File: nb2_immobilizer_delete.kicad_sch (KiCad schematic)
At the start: 6 parts, among them J1 AVR-ISP-6, Q1 BC849, Q2 BC849, U1 ATtiny85-20S

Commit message: first draft
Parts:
- added P1: 1123038-2, 1123038-2:1123038-2, symbol 1123038-2:1123038-2
- J1: footprint Package_SO:SOIC-20W_7.5x12.8mm_P1.27mm -> Connector:Tag-Connect_TC2030-IDC-NL_2x03_P1.27mm_Vertical
- Q1, Q2: LCSC Part # (none) -> C334244
- R1: footprint Resistor_THT:R_Array_SIP4 -> Resistor_SMD:R_0603_1608Metric; LCSC Part # (none) -> C22807
- R2: footprint Resistor_THT:R_Array_SIP4 -> Resistor_SMD:R_0603_1608Metric; LCSC Part # (none) -> C22843
- U1: LCSC Part # (none) -> C31540447
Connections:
- net +5V: now also P1.66 (4L)
- net GND: now also P1.64 (4A)
- net bus: now also P1.36 (3S)
- net cluster: no longer names the net of U1.3 (XTAL2/PB4)
- net led renamed PB1
- no-connect marks 1 -> 71
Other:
- moved on the sheet: J1, Q1, Q2, R1, R2, U1

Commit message: added capacitor, dnp tag-connect
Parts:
- added C1: 100nf, Capacitor_SMD:C_0603_1608Metric, symbol Device:C_Small
- J1: now left out of the parts list
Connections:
- net +5V: now also C1.1
- net GND: now also C1.2
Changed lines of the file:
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@@
 		(body_style 1)
 		(exclude_from_sim no)
-		(in_bom yes)
-		(on_board yes)
-		(in_pos_files yes)
+		(in_bom no)
+		(on_board yes)
+		(in_pos_files no)
 		(dnp no)
 		(property "Reference" "J1"
@@
 				(path "/20eccbaf-1c27-4c38-b279-b161e9ceabac"
 					(reference "J1")
+					(unit 1)
+				)
+			)
+		)
+	)
+	(symbol
+		(lib_id "Device:C_Small")
+		(at 52.07 54.61 0)
+		(unit 1)
+		(body_style 1)
+		(exclude_from_sim no)
+		(in_bom yes)
+		(on_board yes)
+		(in_pos_files yes)
+		(dnp no)
+		(fields_autoplaced yes)
+		(property "Reference" "C1"
+			(at 54.61 53.3399 0)
+			(show_name no)
+			(do_not_autoplace no)
+			(effects
+				(font
+					(size 1.27 1.27)
+				)
+				(justify left)
+			)
+		)
+		(property "Value" "100nf"
+			(at 54.61 55.8799 0)
+			(show_name no)
+			(do_not_autoplace no)
+			(effects
+				(font
+					(size 1.27 1.27)
+				)
+				(justify left)
+			)
+		)
+		(property "Footprint" "Capacitor_SMD:C_0603_1608Metric"
+			(at 52.07 54.61 0)
+			(hide yes)
+			(show_name no)
+			(do_not_autoplace no)
+			(effects
+				(font
+					(size 1.27 1.27)
+				)
+			)
+		)
+		(property "Datasheet" ""
+			(at 52.07 54.61 0)
+			(hide yes)
+			(show_name no)
+			(do_not_autoplace no)
+			(effects
+				(font
+					(size 1.27 1.27)
+				)
+			)
+		)
+		(property "Description" "Unpolarized capacitor, small symbol"
+			(at 52.07 64.77 0)
+			(hide yes)
+			(show_name no)
+			(do_not_autoplace no)
+			(effects
+				(font
+					(size 1.27 1.27)
+				)
+			)
+		)
+		(pin "1"
+		)
+		(pin "2"
+		)
+		(instances
+			(project "nb2_immobilizer_delete"
+				(path "/20eccbaf-1c27-4c38-b279-b161e9ceabac"
+					(reference "C1")
 					(unit 1)
 				)
@@
 	)
 	(symbol
+		(lib_id "power:GND")
+		(at 52.07 57.15 0)
+		(unit 1)
+		(body_style 1)
+		(exclude_from_sim no)
+		(in_bom yes)
+		(on_board yes)
+		(in_pos_files yes)
+		(dnp no)
+		(fields_autoplaced yes)
+		(property "Reference" "#PWR010"
+			(at 52.07 63.5 0)
+			(hide yes)
+			(show_name no)
+			(do_not_autoplace no)
+			(effects
+				(font
+					(size 1.27 1.27)
+				)
+			)
+		)
+		(property "Value" "GND"
+			(at 52.07 62.23 0)
+			(show_name no)
+			(do_not_autoplace no)
+			(effects
+				(font
+					(size 1.27 1.27)
+				)
+			)
+		)
+		(property "Footprint" ""
+			(at 52.07 57.15 0)
+			(hide yes)
+			(show_name no)
+			(do_not_autoplace no)
+			(effects
+				(font
+					(size 1.27 1.27)
+				)
+			)
+		)
+		(property "Datasheet" ""
+			(at 52.07 57.15 0)
+			(hide yes)
+			(show_name no)
+			(do_not_autoplace no)
+			(effects
+				(font
+					(size 1.27 1.27)
+				)
+			)
+		)
+		(property "Description" "Power symbol creates a global label with name \"GND\" , ground"
+			(at 52.07 57.15 0)
+			(hide yes)
+			(show_name no)
+			(do_not_autoplace no)
+			(effects
+				(font
+					(size 1.27 1.27)
+				)
+			)
+		)
+		(pin "1"
+		)
+		(instances
+			(project "nb2_immobilizer_delete"
+				(path "/20eccbaf-1c27-4c38-b279-b161e9ceabac"
+					(reference "#PWR010")
+					(unit 1)
+				)
+			)
+		)
+	)
+	(symbol
 		(lib_id "Device:R_Small")
 		(at 96.52 57.15 180)
@@
 					(unit 1)
 				)
+			)
+		)
+	)
+	(symbol
+		(lib_id "power:+5V")
+		(at 52.07 52.07 0)
+		(unit 1)
+		(body_style 1)
+		(exclude_from_sim no)
+		(in_bom yes)
+		(on_board yes)
+		(in_pos_files yes)
+		(dnp no)
+		(fields_autoplaced yes)
+		(property "Reference" "#PWR09"
+			(at 52.07 55.88 0)
+			(hide yes)
+			(show_name no)
+			(do_not_autoplace no)
+			(effects
+				(font
+					(size 1.27 1.27)
+				)
+			)
+		)
+		(property "Value" "+5V"
+			(at 52.07 46.99 0)
+			(show_name no)
+			(do_not_autoplace no)
+			(effects
+				(font
+					(size 1.27 1.27)
+				)
+			)
+		)
+		(property "Footprint" "Package_SO:SOIC-8_5.3x5.3mm_P1.27mm"
+			(at 52.07 52.07 0)
+			(hide yes)
+			(show_name no)
+			(do_not_autoplace no)
+			(effects
+				(font
+					(size 1.27 1.27)
+				)
+			)
+		)
+		(property "Datasheet" ""
+			(at 52.07 52.07 0)
+			(hide yes)
+			(show_name no)
+			(do_not_autoplace no)
+			(effects
+				(font
+					(size 1.27 1.27)
+				)
+			)
+		)
+		(property "Description" "Power symbol creates a global label with name \"+5V\""
+			(at 52.07 52.07 0)
+			(hide yes)
+			(show_name no)
+			(do_not_autoplace no)
+			(effects
+				(font
+					(size 1.27 1.27)
+				)
+			)
+		)
+		(pin "1"
+		)
+		(instances
+			(project "nb2_immobilizer_delete"
+				(path "/20eccbaf-1c27-4c38-b279-b161e9ceabac"
+					(reference "#PWR09")
+					(unit 1)
+				)

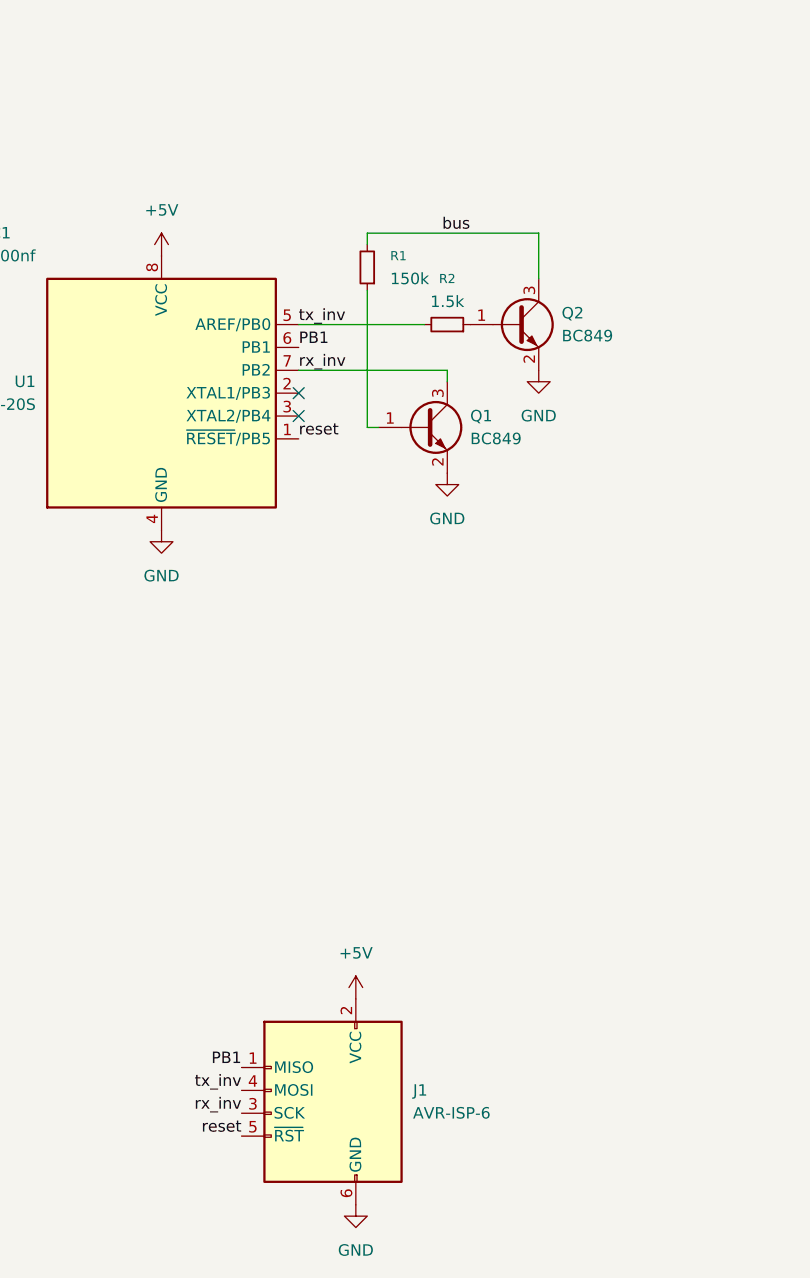
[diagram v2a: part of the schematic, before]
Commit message: revised layout for robustness, reduced clock to 1mhz, added github actions workflow
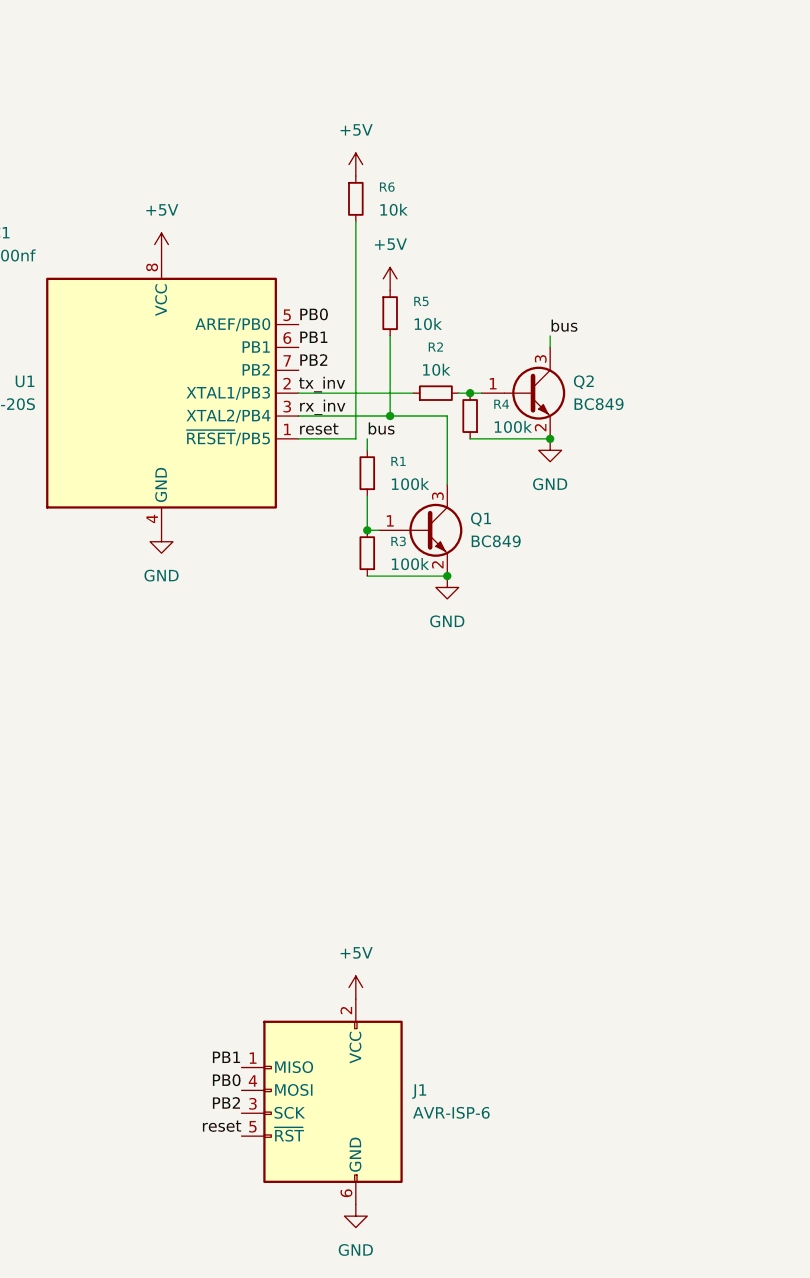
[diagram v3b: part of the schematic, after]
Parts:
- added R3, R4: 100k, Resistor_SMD:R_0603_1608Metric, symbol Device:R_Small
- added R5, R6: 10k, Resistor_SMD:R_0603_1608Metric, symbol Device:R_Small
- R1: value 150k -> 100k; LCSC Part # C22807 -> C25803
- R2: value 1.5k -> 10k; LCSC Part # C22843 -> C25804
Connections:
- net +5V: now also R5.1, R6.1
- net GND: now also R3.1, R4.1
- net reset: now also R6.2
- net rx_inv: now also U1.3 (XTAL2/PB4), R5.2; no longer J1.3 (SCK), U1.7 (PB2)
- net tx_inv: now also R2.1, U1.2 (XTAL1/PB3); no longer J1.4 (MOSI), R2.2, U1.5 (AREF/PB0)
- net at Q2.1 (B): now also R2.2, R4.2; no longer R2.1
- net at Q1.1 (B), R1.1: now also R3.2
- new net PB0: J1.4 (MOSI), U1.5 (AREF/PB0)
- new net PB2: J1.3 (SCK), U1.7 (PB2)
- no-connect marks 71 -> 69
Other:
- moved on the sheet: Q1, Q2, R1
